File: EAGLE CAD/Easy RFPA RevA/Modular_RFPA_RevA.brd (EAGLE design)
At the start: 152.4 x 152.4 mm, 197 parts, among them IC401 LDO_3TERMMC78M12CTGTO220_VERT, IC402 LDO_3TERMMC78M05CTGTO220_VERT, J401 FUSE_2P, J402 KK_PCFAN, Q101 IRF520N, Q102 IRF630, Q201 IRF630, Q202 IRF630, Q301 MOSFET_NBSS123SOT23, Q302 PNPSOT23_BEC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

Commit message: Do same for capacitor library
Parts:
- C114, C115, C211, C212: value 10nF -> 0.1uF
- C201, C203: value 22nF -> 0.1uF
- C202, C204: value 27nF -> 0.1uF
- C205, C206, C207, C208, C302, C303: value DNP -> 0.1uF
- C304: value 33pF -> 0.1uF

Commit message: More part attributes....
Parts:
- removed X401: (no value), con-wago-500:W237-102
- added J1: HDR_2X1282836-1282836-1, MDT_CON:W237-02
- C114, C115, C211, C212: value 0.1uF -> 10nF
- C201, C203: value 0.1uF -> 22nF
- C202, C204: value 0.1uF -> 27nF
- C205, C206, C207, C208, C302, C303: value 0.1uF -> DNP
- C209, C210: value 22nF -> 2.2nF
- C304: value 0.1uF -> 33pF
- C406, C407: value 47nF -> 4.7uF
- J101, J102, J301, J302: value (none) -> COAX112640BNC_EDGE
- R130, R131: value (none) -> 10K
- R301: device rcl:RTRIM3299W -> MDT_R:RTRIM3299W
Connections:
- net GND: now also J1.2; no longer X401.2
- net N$45: now also J1.1; no longer X401.1

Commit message: EXCLUDEs and INCLUDEs
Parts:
- renumbered IC401 to U401, IC402 to U402

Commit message: bom-ex export working
Need to use tab-delimited format due to parts with commas in partno....
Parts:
- R130, R131: value 10K -> 1K
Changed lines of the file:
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@@
 <attribute name="PACKAGE" value="1008" x="67.564" y="92.71" size="1.778" layer="27" rot="R180" display="off"/>
 <attribute name="IDC" value="1A" x="67.564" y="92.71" size="1.778" layer="27" rot="R180" display="off"/>
-<attribute name="PARTNO" value="1008CS-470XJEC" x="67.564" y="92.71" size="1.778" layer="27" rot="R180" display="off"/>
+<attribute name="PARTNO" value="1008CS-470XJLC" x="67.564" y="92.71" size="1.778" layer="27" rot="R180" display="off"/>
 <attribute name="ISAT" value="" x="67.564" y="92.71" size="1.778" layer="27" rot="R180" display="off"/>
 <attribute name="BOM" value="INCLUDE" x="67.564" y="92.71" size="1.778" layer="27" rot="R180" display="off"/>
@@
 <attribute name="VENDOR" value="" x="111.76" y="68.58" size="1.778" layer="27" rot="R180" display="off"/>
 </element>
-<element name="U301" library="74xx-little-us" package="SOT23-5" value="74AHC1G14DBV" x="76.2" y="19.05"/>
+<element name="U301" library="74xx-little-us" package="SOT23-5" value="74AHC1G14DBV" x="76.2" y="19.05">
+<attribute name="BOM" value="INCLUDE" x="76.2" y="19.05" size="1.778" layer="27" display="off"/>
+<attribute name="PARTNO" value="74AHC1G14QW5-7" x="76.2" y="19.05" size="1.778" layer="27" display="off"/>
+<attribute name="VENDOR" value="Diodes Inc" x="76.2" y="19.05" size="1.778" layer="27" display="off"/>
+<attribute name="DESCRIPTION" value="IC INVERT SCHMITT 1CH 1-IN SOT25" x="76.2" y="19.05" size="1.778" layer="27" display="off"/>
+<attribute name="PACKAGE" value="SOT23-5" x="76.2" y="19.05" size="1.778" layer="27" display="off"/>
+</element>
 <element name="R120" library="MDT_R" package="R2512" value="2.74K" x="65.532" y="87.63" rot="R180">
 <attribute name="PACKAGE" value="2512" x="65.532" y="87.63" size="1.778" layer="27" rot="R180" display="off"/>
@@
 <variant name="IRF630_200W" populate="no"/>
 </element>
-<element name="R131" library="MDT_R" package="0805_IPC-7351B" value="10K" x="63.754" y="110.49">
+<element name="R131" library="MDT_R" package="0805_IPC-7351B" value="1K" x="63.754" y="110.49">
 <attribute name="PACKAGE" value="0805" x="63.754" y="110.49" size="1.778" layer="27" display="off"/>
 <attribute name="PARTNO" value="" x="63.754" y="110.49" size="1.778" layer="27" display="off"/>
@@
 <attribute name="PACKAGE" value="1008" x="29.464" y="89.154" size="1.778" layer="27" display="off"/>
 <attribute name="IDC" value="1A" x="29.464" y="89.154" size="1.778" layer="27" display="off"/>
-<attribute name="PARTNO" value="1008CS-470XJEC" x="29.464" y="89.154" size="1.778" layer="27" display="off"/>
+<attribute name="PARTNO" value="1008CS-470XJLC" x="29.464" y="89.154" size="1.778" layer="27" display="off"/>
 <attribute name="ISAT" value="" x="29.464" y="89.154" size="1.778" layer="27" display="off"/>
 <attribute name="BOM" value="INCLUDE" x="29.464" y="89.154" size="1.778" layer="27" display="off"/>
@@
 <variant name="IRF630_200W" populate="no"/>
 </element>
-<element name="R130" library="MDT_R" package="0805_IPC-7351B" value="10K" x="37.846" y="80.01" rot="R180">
+<element name="R130" library="MDT_R" package="0805_IPC-7351B" value="1K" x="37.846" y="80.01" rot="R180">
 <attribute name="PACKAGE" value="0805" x="52.578" y="119.634" size="1.778" layer="27" rot="R180" display="off"/>
 <attribute name="PARTNO" value="" x="52.578" y="119.634" size="1.778" layer="27" rot="R180" display="off"/>
@@
 <attribute name="PACKAGE" value="1008" x="67.564" y="54.61" size="1.778" layer="27" rot="R180" display="off"/>
 <attribute name="IDC" value="1A" x="67.564" y="54.61" size="1.778" layer="27" rot="R180" display="off"/>
-<attribute name="PARTNO" value="1008CS-470XJEC" x="67.564" y="54.61" size="1.778" layer="27" rot="R180" display="off"/>
+<attribute name="PARTNO" value="1008CS-470XJLC" x="67.564" y="54.61" size="1.778" layer="27" rot="R180" display="off"/>
 <attribute name="ISAT" value="" x="67.564" y="54.61" size="1.778" layer="27" rot="R180" display="off"/>
 <attribute name="BOM" value="INCLUDE" x="67.564" y="54.61" size="1.778" layer="27" rot="R180" display="off"/>
@@
 <attribute name="PACKAGE" value="1008" x="29.464" y="51.054" size="1.778" layer="27" display="off"/>
 <attribute name="IDC" value="1A" x="29.464" y="51.054" size="1.778" layer="27" display="off"/>
-<attribute name="PARTNO" value="1008CS-470XJEC" x="29.464" y="51.054" size="1.778" layer="27" display="off"/>
+<attribute name="PARTNO" value="1008CS-470XJLC" x="29.464" y="51.054" size="1.778" layer="27" display="off"/>
 <attribute name="ISAT" value="" x="29.464" y="51.054" size="1.778" layer="27" display="off"/>
 <attribute name="BOM" value="INCLUDE" x="29.464" y="51.054" size="1.778" layer="27" display="off"/>

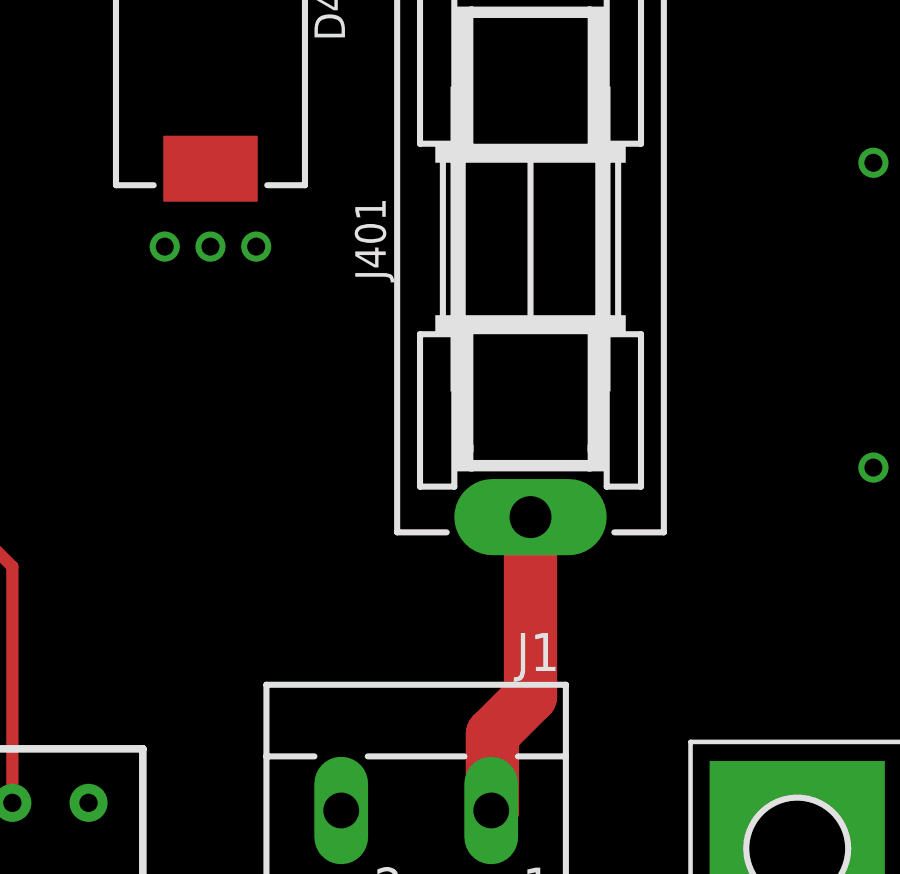
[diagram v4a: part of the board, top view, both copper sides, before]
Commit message: Tidying up revA schematic
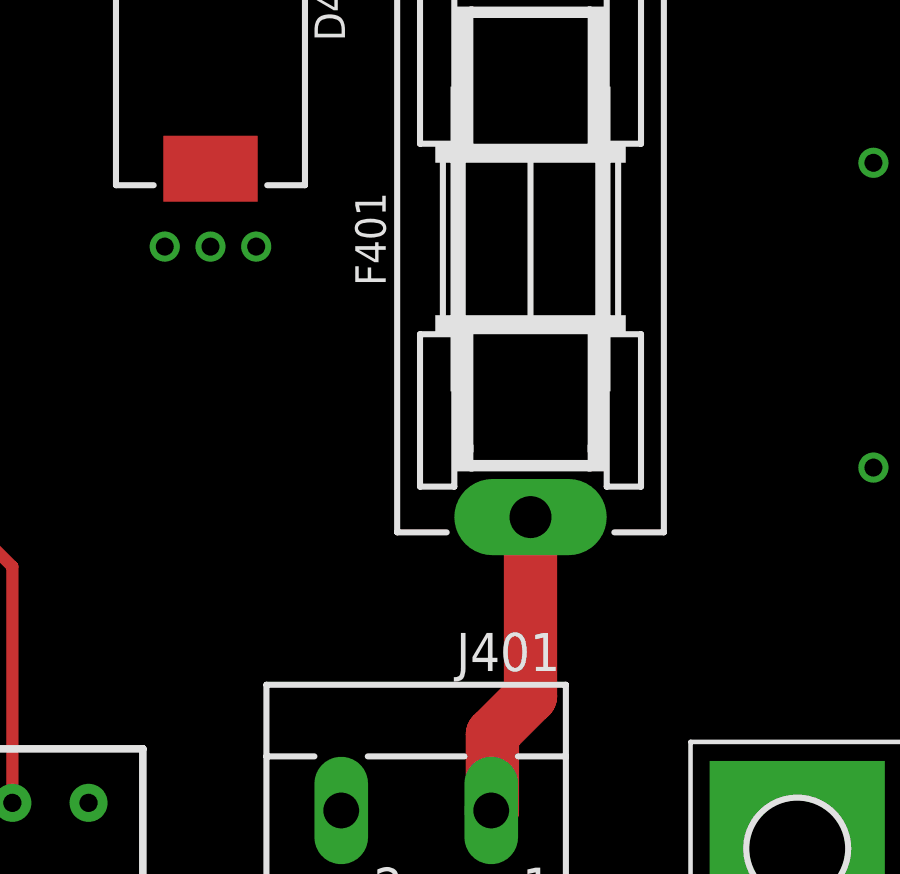
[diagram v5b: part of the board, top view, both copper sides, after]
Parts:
- removed J1: HDR_2X1282836-1282836-1, MDT_CON:W237-02
- added F401: FUSE_2P, MDT_FUSE:02540121Z
- J401: value FUSE_2P -> HDR_2X1282836-1282836-1; device MDT_FUSE:02540121Z -> MDT_CON:W237-02
- moved J401 20.7 mm to (134.6, 5.08), turned to 180 degrees
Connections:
- net GND: now also J401.2; no longer J1.2
- net N$44: now also F401.2; no longer J401.2
- net N$45: now also F401.1; no longer J1.1
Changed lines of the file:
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@@
 <attribute name="VENDOR" value="Wakefield-Vette" x="50.8" y="76.2" size="1.778" layer="27" display="off"/>
 <attribute name="BOM" value="INCLUDE" x="50.8" y="76.2" size="1.778" layer="27" display="off"/>
+<attribute name="DESCRIPTION" value="HEATSINK TO-247 TO-264 TO-220" x="50.8" y="76.2" size="1.778" layer="27" display="off"/>
 </element>
 <element name="R103" library="MDT_R" package="1206_IPC-7351B" value="75" x="82.296" y="96.774" rot="R90">
@@
 <attribute name="BOM" value="INCLUDE" x="50.8" y="25.4" size="1.778" layer="27" display="off"/>
 </element>
-<element name="J401" library="MDT_FUSE" package="02540121Z" value="FUSE_2P" x="138.43" y="25.4" rot="R90">
+<element name="F401" library="MDT_FUSE" package="02540121Z" value="FUSE_2P" x="138.43" y="25.4" rot="R90">
 <attribute name="PARTNO" value="02540121Z" x="138.43" y="25.4" size="1.778" layer="27" rot="R90" display="off"/>
 <attribute name="BOM" value="INCLUDE" x="138.43" y="25.4" size="1.778" layer="27" rot="R90" display="off"/>
@@
 <variant name="IRF630_200W"/>
 </element>
-<element name="J1" library="MDT_CON" package="W237-02" value="HDR_2X1282836-1282836-1" x="134.62" y="5.08" rot="R180">
+<element name="J401" library="MDT_CON" package="W237-02" value="HDR_2X1282836-1282836-1" x="134.62" y="5.08" rot="R180">
 <attribute name="PARTNO" value="282836-1" x="134.62" y="5.08" size="1.778" layer="27" rot="R180" display="off"/>
 <attribute name="DESCRIPTION" value="TERM BLK 2POS SIDE ENTRY 5MM PCB" x="134.62" y="5.08" size="1.778" layer="27" rot="R180" display="off"/>
@@
 <via x="19.05" y="86.106" extent="1-16" drill="0.381"/>
 <via x="20.32" y="48.006" extent="1-16" drill="0.381"/>
-<contactref element="J1" pad="2"/>
+<contactref element="J401" pad="2"/>
 <wire x1="134.112" y1="110.236" x2="134.62" y2="118.11" width="0" layer="19" extent="1-1"/>
 <wire x1="134.112" y1="108.712" x2="134.112" y2="110.236" width="0" layer="19" extent="1-1"/>
@@
 <contactref element="D401" pad="K"/>
 <contactref element="R401" pad="1"/>
-<contactref element="J401" pad="2"/>
+<contactref element="F401" pad="2"/>
 <wire x1="138.43" y1="34.671" x2="138.43" y2="41.91" width="1.778" layer="1"/>
 <wire x1="138.43" y1="34.671" x2="128.033" y2="34.671" width="1.778" layer="1"/>
@@
 </signal>
 <signal name="N$45">
-<contactref element="J401" pad="1"/>
+<contactref element="F401" pad="1"/>
 <wire x1="138.43" y1="16.129" x2="138.43" y2="10.16" width="1.778" layer="1"/>
 <wire x1="138.43" y1="10.16" x2="137.16" y2="8.89" width="1.778" layer="1"/>
-<contactref element="J1" pad="1"/>
+<contactref element="J401" pad="1"/>
 <wire x1="137.12" y1="6.35" x2="137.16" y2="6.35" width="1.778" layer="1"/>
 <wire x1="137.16" y1="6.35" x2="137.16" y2="8.89" width="1.778" layer="1"/>
